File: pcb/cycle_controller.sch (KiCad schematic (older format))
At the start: 49 parts

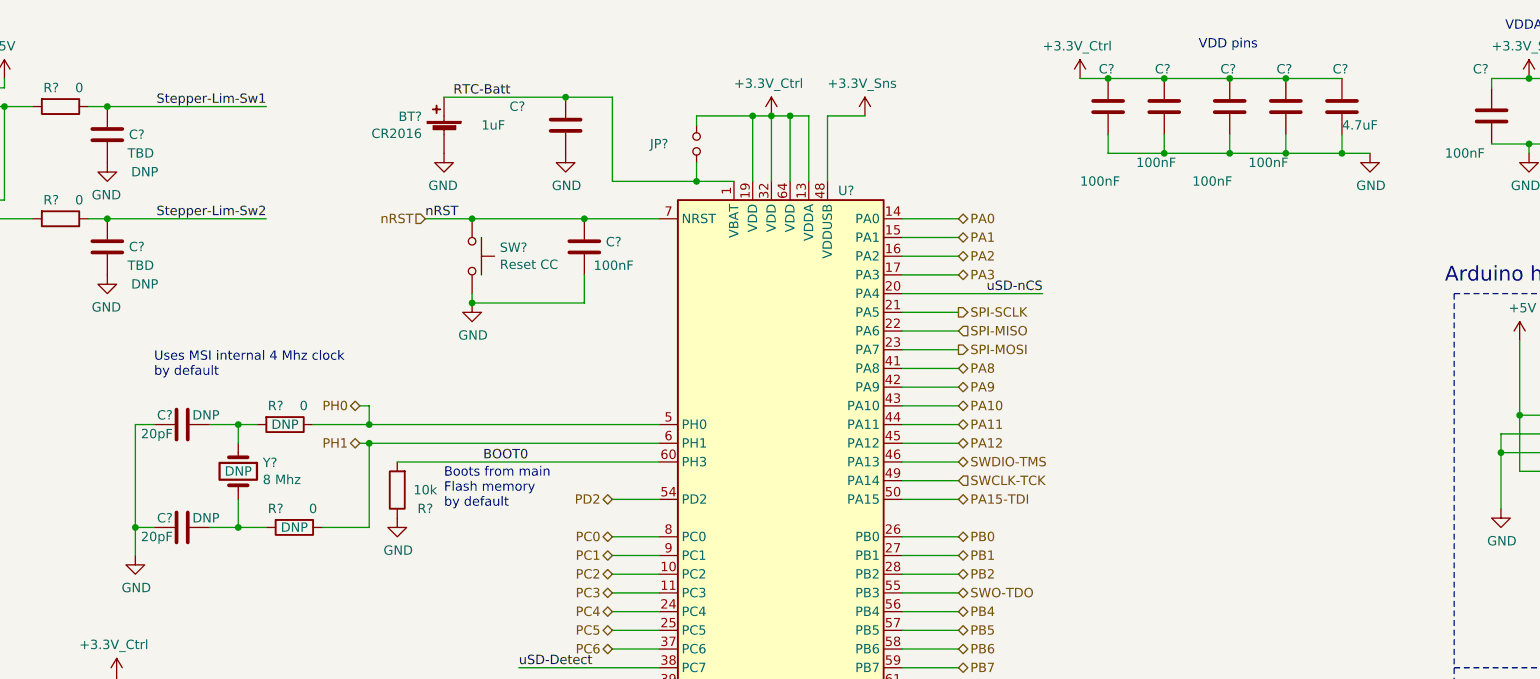
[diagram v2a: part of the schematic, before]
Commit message: BOM
More BOM consolidation with bulk capacitors + changed tantalum stepper caps to aluminum, added bulk cap to PSol driver
Made stepper's 3.3V power naming consistent with others (3.3V->3V3)
Slightly increased current limit on PSOL/heater driver
Changed 3906 transistors to 2907 to better support +5V_Batt current
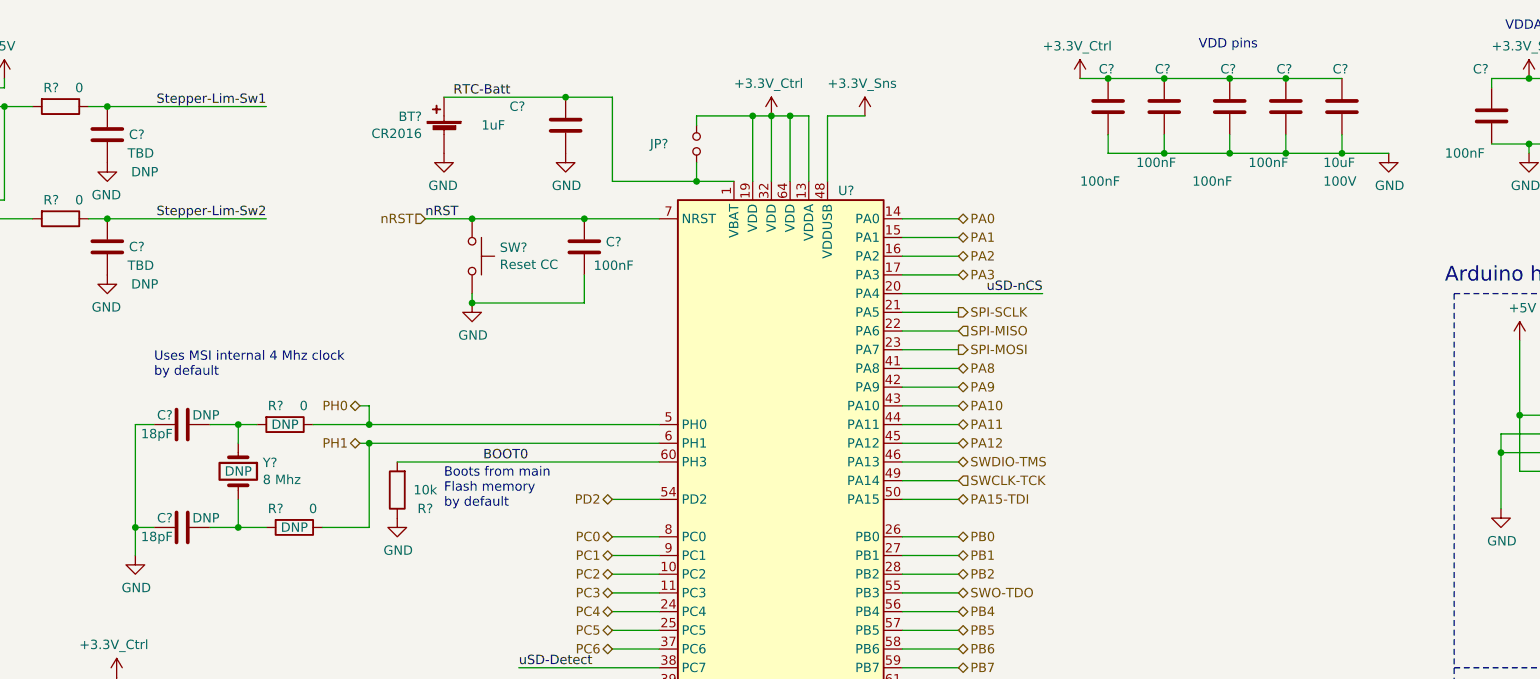
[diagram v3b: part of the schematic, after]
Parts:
- removed C?: 4.7uF, RespiraWorks_Std:C_0603_1608Metric, symbol Device:C
- added C?: 10uF, RespiraWorks_Std:C_1210_3225Metric, symbol Device:C
- C? (x2): value 20pF -> 18pF; Dielectric (none) -> NP0
- C? (x2): footprint RespiraWorks_std:C_0603_1608Metric -> RespiraWorks_Std:C_0603_1608Metric
- R? (x8): footprint RespiraWorks_std:R_0603_1608Metric -> RespiraWorks_Std:R_0603_1608Metric
- TP? (x4): footprint (none) -> RespiraWorks_Std:TestPoint_Pad_2.0x2.0mm
- Y?: Manufacturer (none) -> Abracon; Manufacturer PN (none) -> ABLS-8.000MHZ-B4-T
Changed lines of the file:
@@
-	1    0    0    -1
-$EndComp
-$Comp
-L Device:C C?
-U 1 1 5FEBCA35
-P 8750 1000
-F 0 "C?" H 8700 1200 50  0000 L CNN
-F 1 "4.7uF" H 8750 900 50  0000 L CNN
-F 2 "RespiraWorks_Std:C_0603_1608Metric" H 8788 850 50  0001 C CNN
-F 3 "~" H 8750 1000 50  0001 C CNN
-	1    8750 1000
 	1    0    0    -1
 $EndComp
@@
 L power:GND #PWR?
 U 1 1 5FEBCB86
-P 8900 1250
-F 0 "#PWR?" H 8900 1000 50  0001 C CNN
-F 1 "GND" H 8905 1077 50  0000 C CNN
-F 2 "" H 8900 1250 50  0001 C CNN
-F 3 "" H 8900 1250 50  0001 C CNN
-	1    8900 1250
+P 9000 1250
+F 0 "#PWR?" H 9000 1000 50  0001 C CNN
+F 1 "GND" H 9005 1077 50  0000 C CNN
+F 2 "" H 9000 1250 50  0001 C CNN
+F 3 "" H 9000 1250 50  0001 C CNN
+	1    9000 1250
 	1    0    0    -1
 $EndComp
@@
 F 3 "~" H 2850 2950 50  0001 C CNN
 F 4 "DNP" V 2850 2950 50  0000 C CNN "DNP"
+F 5 "Abracon" H 2850 2950 50  0001 C CNN "Manufacturer"
+F 6 "ABLS-8.000MHZ-B4-T" H 2850 2950 50  0001 C CNN "Manufacturer PN"
 	1    2850 2950
 	0    1    1    0
@@
 P 2550 2700
 F 0 "C?" V 2600 2750 50  0000 L CNN
-F 1 "20pF" V 2500 2750 50  0000 L CNN
+F 1 "18pF" V 2500 2750 50  0000 L CNN
 F 2 "RespiraWorks_Std:C_0603_1608Metric" H 2588 2550 50  0001 C CNN
 F 3 "~" H 2550 2700 50  0001 C CNN
 F 4 "DNP" V 2600 2500 50  0000 L CNN "DNP"
+F 5 "NP0" H 2550 2700 50  0001 C CNN "Dielectric"
 	1    2550 2700
 	0    -1   -1   0
@@
 P 2550 3250
 F 0 "C?" V 2600 3300 50  0000 L CNN
-F 1 "20pF" V 2500 3300 50  0000 L CNN
+F 1 "18pF" V 2500 3300 50  0000 L CNN
 F 2 "RespiraWorks_Std:C_0603_1608Metric" H 2588 3100 50  0001 C CNN
 F 3 "~" H 2550 3250 50  0001 C CNN
 F 4 "DNP" V 2600 3050 50  0000 L CNN "DNP"
+F 5 "NP0" H 2550 3250 50  0001 C CNN "Dielectric"
 	1    2550 3250
 	0    -1   -1   0
@@
 F 0 "R?" V 3000 2650 50  0000 C CNN
 F 1 "0" V 3000 2800 50  0000 C CNN
-F 2 "RespiraWorks_std:R_0603_1608Metric" V 3030 2700 50  0001 C CNN
+F 2 "RespiraWorks_Std:R_0603_1608Metric" V 3030 2700 50  0001 C CNN
 F 3 "~" H 3100 2700 50  0001 C CNN
 F 4 "DNP" V 3100 2700 50  0000 C CNN "DNP"
@@
 F 0 "R?" V 3050 3150 50  0000 C CNN
 F 1 "0" V 3050 3350 50  0000 C CNN
-F 2 "RespiraWorks_std:R_0603_1608Metric" V 3080 3250 50  0001 C CNN
+F 2 "RespiraWorks_Std:R_0603_1608Metric" V 3080 3250 50  0001 C CNN
 F 3 "~" H 3150 3250 50  0001 C CNN
 F 4 "DNP" V 3150 3250 50  0000 C CNN "DNP"
@@
 F 0 "R?" V 4350 4950 50  0000 C CNN
 F 1 "0" V 4350 5150 50  0000 C CNN
-F 2 "RespiraWorks_std:R_0603_1608Metric" V 4380 5050 50  0001 C CNN
+F 2 "RespiraWorks_Std:R_0603_1608Metric" V 4380 5050 50  0001 C CNN
 F 3 "~" H 4450 5050 50  0001 C CNN
 	1    4450 5050
@@
 F 0 "R?" V 4350 4650 50  0000 C CNN
 F 1 "0" V 4350 4800 50  0000 C CNN
-F 2 "RespiraWorks_std:R_0603_1608Metric" V 4380 4700 50  0001 C CNN
+F 2 "RespiraWorks_Std:R_0603_1608Metric" V 4380 4700 50  0001 C CNN
 F 3 "~" H 4450 4700 50  0001 C CNN
 	1    4450 4700
@@
 F 0 "C?" V 3750 5000 50  0000 L CNN
 F 1 "6.8pF" V 3850 4950 50  0000 L CNN
-F 2 "RespiraWorks_std:C_0603_1608Metric" H 3638 4900 50  0001 C CNN
+F 2 "RespiraWorks_Std:C_0603_1608Metric" H 3638 4900 50  0001 C CNN
 F 3 "~" H 3600 5050 50  0001 C CNN
 F 4 "" V 3950 5050 50  0001 C CNN "DNP"
@@
 F 0 "R?" H 4150 5250 50  0000 C CNN
 F 1 "0" H 4150 5350 50  0000 C CNN
-F 2 "RespiraWorks_std:R_0603_1608Metric" V 4180 5250 50  0001 C CNN
+F 2 "RespiraWorks_Std:R_0603_1608Metric" V 4180 5250 50  0001 C CNN
 F 3 "~" H 4250 5250 50  0001 C CNN
 F 4 "DNP" H 4100 5450 50  0000 C CNN "DNP"
@@
 F 0 "R?" H 4200 5250 50  0000 C CNN
 F 1 "0" H 4200 5350 50  0000 C CNN
-F 2 "RespiraWorks_std:R_0603_1608Metric" V 4030 5250 50  0001 C CNN
+F 2 "RespiraWorks_Std:R_0603_1608Metric" V 4030 5250 50  0001 C CNN
 F 3 "~" H 4100 5250 50  0001 C CNN
 F 4 "DNP" H 4200 5450 50  0000 C CNN "DNP"
@@
 Connection ~ 7500 850
 Wire Wire Line
-	8900 1250 8750 1250
+	9000 1250 8750 1250
 Connection ~ 8750 1250
 $Comp
@@
 F 0 "C?" V 3450 4550 50  0000 L CNN
 F 1 "6.8pF" V 3550 4300 50  0000 L CNN
-F 2 "RespiraWorks_std:C_0603_1608Metric" H 3638 4450 50  0001 C CNN
+F 2 "RespiraWorks_Std:C_0603_1608Metric" H 3638 4450 50  0001 C CNN
 F 3 "~" H 3600 4600 50  0001 C CNN
 F 4 "" V 3450 4400 50  0001 C CNN "DNP"
@@
 F 0 "TP?" H 4600 7000 50  0000 C CNN
 F 1 "TP" V 4650 6850 50  0001 C CNN
-F 2 "" H 4800 6800 50  0001 C CNN
+F 2 "RespiraWorks_Std:TestPoint_Pad_2.0x2.0mm" H 4800 6800 50  0001 C CNN
 F 3 "~" H 4800 6800 50  0001 C CNN
 	1    4600 6800
@@
 F 0 "TP?" H 4800 7000 50  0000 C CNN
 F 1 "TP" V 4850 6850 50  0001 C CNN
-F 2 "" H 5000 6800 50  0001 C CNN
+F 2 "RespiraWorks_Std:TestPoint_Pad_2.0x2.0mm" H 5000 6800 50  0001 C CNN
 F 3 "~" H 5000 6800 50  0001 C CNN
 	1    4800 6800
@@
 F 0 "TP?" H 5000 7000 50  0000 C CNN
 F 1 "TP" V 5050 6850 50  0001 C CNN
-F 2 "" H 5200 6800 50  0001 C CNN
+F 2 "RespiraWorks_Std:TestPoint_Pad_2.0x2.0mm" H 5200 6800 50  0001 C CNN
 F 3 "~" H 5200 6800 50  0001 C CNN
 	1    5000 6800
@@
 F 0 "TP?" H 5200 7000 50  0000 C CNN
 F 1 "TP" V 5250 6850 50  0001 C CNN
-F 2 "" H 5400 6800 50  0001 C CNN
+F 2 "RespiraWorks_Std:TestPoint_Pad_2.0x2.0mm" H 5400 6800 50  0001 C CNN
 F 3 "~" H 5400 6800 50  0001 C CNN
 	1    5200 6800
@@
 F 0 "R?" V 1800 950 50  0000 C CNN
 F 1 "0" V 1800 1100 50  0000 C CNN
-F 2 "RespiraWorks_std:R_0603_1608Metric" V 1830 1000 50  0001 C CNN
+F 2 "RespiraWorks_Std:R_0603_1608Metric" V 1830 1000 50  0001 C CNN
 F 3 "~" H 1900 1000 50  0001 C CNN
 	1    1900 1000
@@
 F 0 "R?" V 1800 1550 50  0000 C CNN
 F 1 "0" V 1800 1700 50  0000 C CNN
-F 2 "RespiraWorks_std:R_0603_1608Metric" V 1830 1600 50  0001 C CNN
+F 2 "RespiraWorks_Std:R_0603_1608Metric" V 1830 1600 50  0001 C CNN
 F 3 "~" H 1900 1600 50  0001 C CNN
 	1    1900 1600
@@
 Text Label 4300 4400 0    50   ~ 0
 Stepper-Lim-Sw2
+$Comp
+L Device:C C?
+U 1 1 60471E6F
+P 8750 1000
+AR Path="/601A64F8/60471E6F" Ref="C?"  Part="1"
+AR Path="/601A64F8/60567144/60471E6F" Ref="C?"  Part="1"
+AR Path="/601A64F8/60567D6E/60471E6F" Ref="C?"  Part="1"
+AR Path="/6023BF6A/60567D6E/60471E6F" Ref="C?"  Part="1"
+AR Path="/6041384A/60567D6E/60471E6F" Ref="C?"  Part="1"
+AR Path="/5FCD4B8E/5FCD4BC5/60471E6F" Ref="C?"  Part="1"
+AR Path="/5FCD4B8E/5FE27F70/60471E6F" Ref="C?"  Part="1"
+AR Path="/5FCD4D18/60471E6F" Ref="C?"  Part="1"
+F 0 "C?" H 8700 1200 50  0000 L CNN
+F 1 "10uF" H 8650 700 50  0000 L CNN
+F 2 "RespiraWorks_Std:C_1210_3225Metric" H 8788 850 50  0001 C CNN
+F 3 "~" H 8750 1000 50  0001 C CNN
+F 4 "100V" H 8650 600 50  0000 L CNN "Voltage"
+F 5 "X7S" H 8750 1000 50  0001 C CNN "Dielectric"
+F 6 "Murata" H 8750 1000 50  0001 C CNN "Manufacturer"
+F 7 "GRM32EC72A106KE05L" H 8750 1000 50  0001 C CNN "Manufacturer PN"
+	1    8750 1000
+	1    0    0    -1
+$EndComp
 $EndSCHEMATC

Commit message: added new STM32L496 symbol in the LQFP-100 package
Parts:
- removed U?: STM32L496RGTx, Package_QFP:LQFP-64_10x10mm_P0.5mm, symbol RespiraWorks_Std:STM32L496RGTx
- added C?: 100nF, RespiraWorks_Std:C_0603_1608Metric, symbol Device:C
- added R?: 0, RespiraWorks_Std:R_0603_1608Metric, symbol Device:R
- added U?: STM32L496VGT, Package_QFP:LQFP-100_14x14mm_P0.5mm, symbol RespiraWorks:STM32L496VGT
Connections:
- wire segments 225 -> 240
- no-connect marks 7 -> 38
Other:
- moved on the sheet: C?, J?, JP?, R?, TP?

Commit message: switched LQFP-100 footprint to Respiraworks_std
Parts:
- U?: footprint Package_QFP:LQFP-100_14x14mm_P0.5mm -> RespiraWorks_Std:LQFP-100_14x14mm_P0.5mm
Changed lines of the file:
@@
 F 0 "U?" H 5800 -1100 50  0000 C CNN
 F 1 "STM32L496VGT" H 5800 -1200 50  0000 C CNN
-F 2 "Package_QFP:LQFP-100_14x14mm_P0.5mm" H 6550 -900 50  0001 R CNN
+F 2 "RespiraWorks_Std:LQFP-100_14x14mm_P0.5mm" H 6550 -900 50  0001 R CNN
 F 3 "http://www.st.com/st-web-https://www.st.com/resource/en/datasheet/stm32l496vg.pdf" H 5800 3200 50  0001 C CNN
 	1    5800 3200
